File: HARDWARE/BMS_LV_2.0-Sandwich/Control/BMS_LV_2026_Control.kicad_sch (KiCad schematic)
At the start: 5 parts, among them J1 Conn_01x26

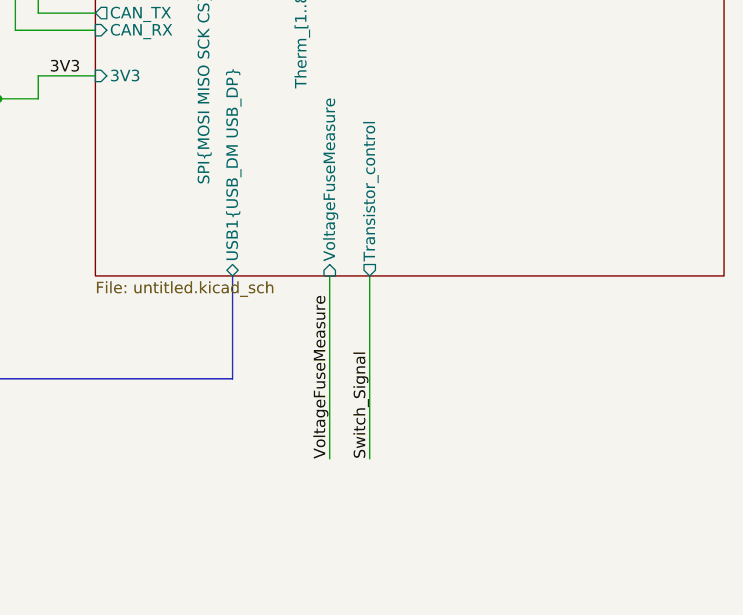
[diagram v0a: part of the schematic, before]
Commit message: Zmiany w power: nowe bezpieczniki, nowy wymienialny layout dla tych bezpiecznikow, dodano diode zenera dla stabilizacji napięcia, zmiany dla control:  wyjebany eeprom, przesunięty can, zmieniony layout przetwornic, dodano programator i tvs, jeszcze do dokonczenia routing w control.
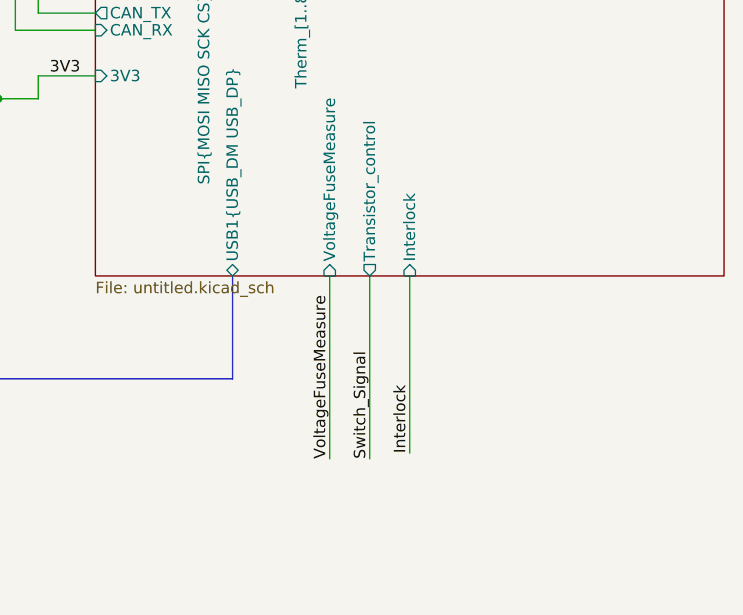
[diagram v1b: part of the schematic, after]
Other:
- sheet Control ports: added Interlock; removed none
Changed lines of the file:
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@@
+	(wire
+		(pts
+			(xy 168.275 117.475) (xy 168.275 137.16)
+		)
+		(stroke
+			(width 0)
+			(type default)
+		)
+	)
 	(wire
 		(pts
@@
 			)
 			(justify right bottom)
+		)
+	)
+	(label "Interlock"
+		(at 168.275 137.16 90)
+		(effects
+			(font
+				(size 1.27 1.27)
+			)
+			(justify left bottom)
 		)
 	)
@@
 			(effects
 				(font
+					(size 1.27 1.27)
+				)
+				(justify left)
+			)
+		)
+		(pin "Interlock" input
+			(at 168.275 117.475 270)
+			(effects
+				(font

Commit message: Ulozono silkscreena
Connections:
- net Therm_1: no longer names the net of J1.5 (Pin_5)
- net Therm_2: no longer names the net of J1.6 (Pin_6)
- net Therm_3: no longer names the net of J1.7 (Pin_7)
- net Therm_4: no longer names the net of J1.8 (Pin_8)
- net Therm_5: no longer names the net of J1.9 (Pin_9)
- net Therm_6: no longer names the net of J1.10 (Pin_10)
- net Therm_7: no longer names the net of J1.11 (Pin_11)
- net Therm_8: no longer names the net of J1.12 (Pin_12)
- no-connect marks 1 -> 9
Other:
- added sheet Thermistors (Thermistors.kicad_sch)
- sheet Control ports: added 3V3A; removed none
- sheet Power ports: added 3V3A; removed none
- moved on the sheet: H1, H2, H3, H4

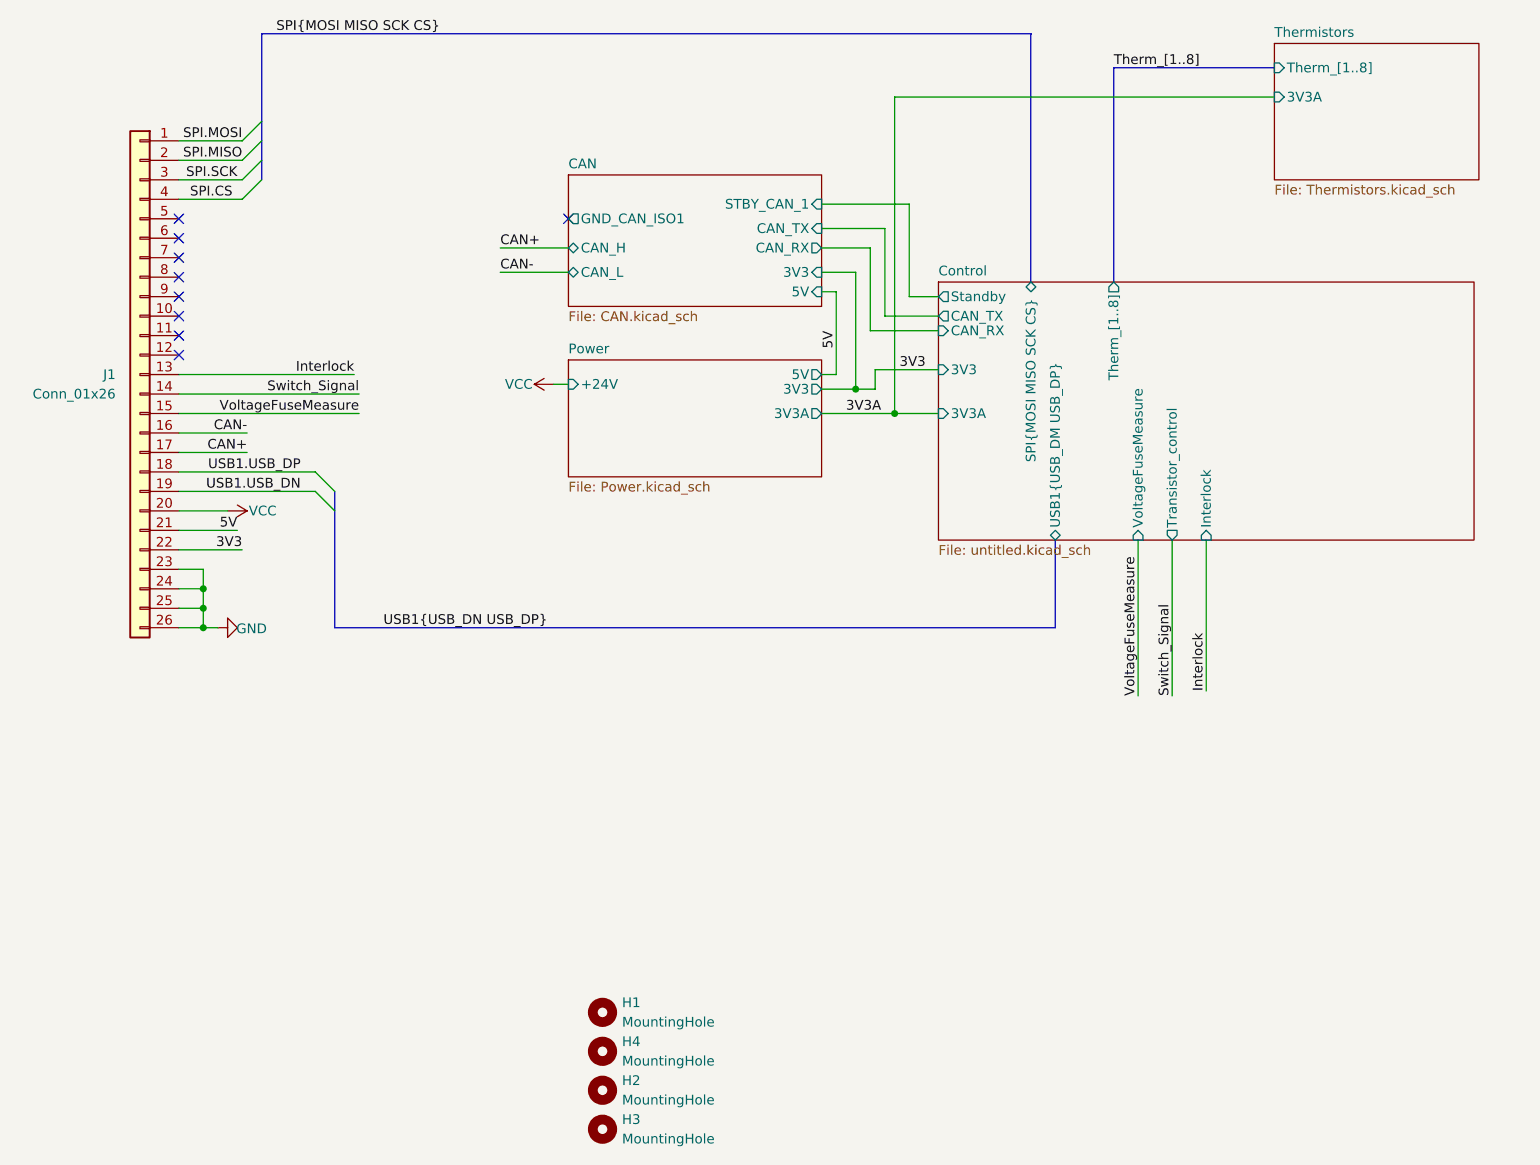
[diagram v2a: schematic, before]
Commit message: Naprawiono: załączanie lv, brak zlącza programatora (XD) oraz brak podłączenia czujnika prądu :9
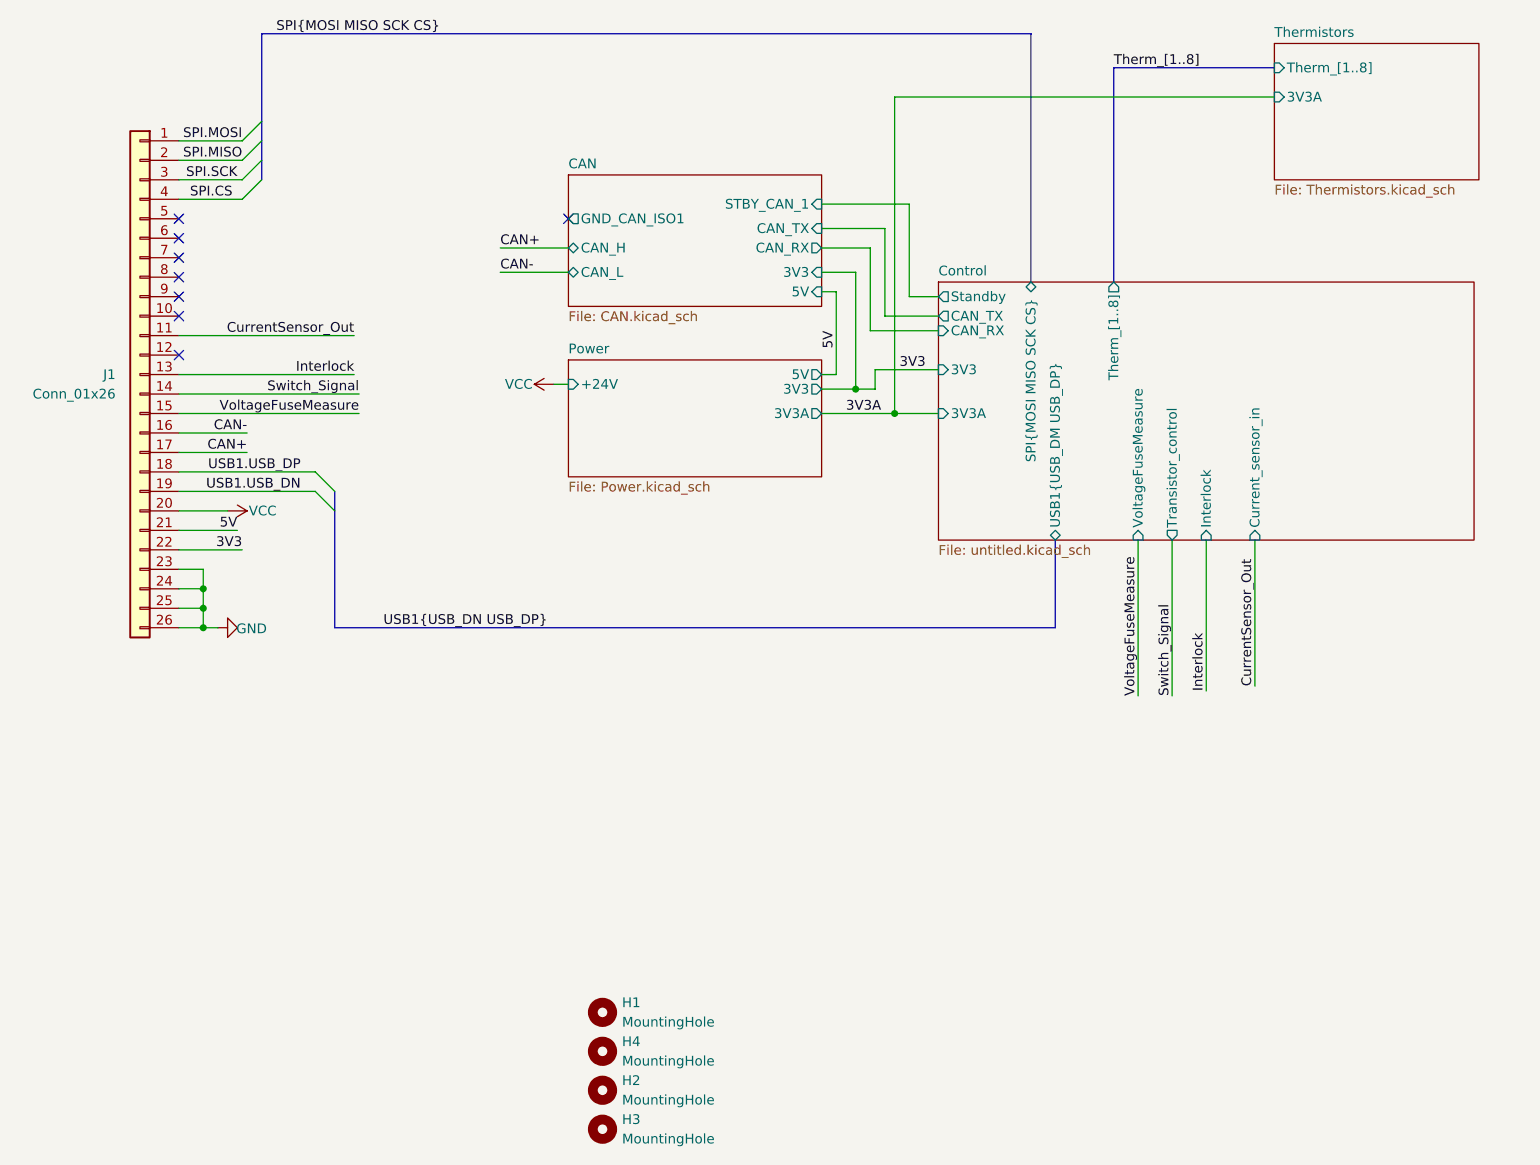
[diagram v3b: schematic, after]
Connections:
- net CurrentSensor_Out: now reaches J1.11 (Pin_11)
- no-connect marks 9 -> 8
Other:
- sheet Control ports: added Current_sensor_in; removed none
